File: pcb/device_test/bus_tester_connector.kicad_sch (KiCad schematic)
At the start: 7 parts, among them J301 USB_C_Receptacle_USB2.0_16P, J302 Conn_02x10_Row_Letter_First

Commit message: update ALL parts
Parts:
- C301: footprint Capacitor_Tantalum_SMD:CP_EIA-7343-43_Kemet-X_Pad2.25x2.55mm_HandSolder -> Capacitor_Tantalum_SMD:CP_EIA-7343-43_Kemet-X; LCSC C7230 -> C132558
- J302: MOUSER (none) -> 798-PCN10C20S254DS72
- R303: value 390 -> 1k; LCSC C17655 -> C17513
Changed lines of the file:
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@@
 			)
 		)
-		(property "Footprint" "Capacitor_Tantalum_SMD:CP_EIA-7343-43_Kemet-X_Pad2.25x2.55mm_HandSolder"
+		(property "Footprint" "Capacitor_Tantalum_SMD:CP_EIA-7343-43_Kemet-X"
 			(at 122.8852 67.31 0)
 			(effects
@@
 			)
 		)
-		(property "LCSC" "C7230"
+		(property "LCSC" "C132558"
 			(at 121.92 63.5 0)
 			(effects
@@
 				)
 				(hide yes)
+			)
+		)
+		(property "MOUSER" ""
+			(at 121.92 63.5 0)
+			(effects
+				(font
+					(size 1.27 1.27)
+				)
 			)
 		)
@@
 			)
 		)
-		(property "Value" "390"
+		(property "Value" "1k"
 			(at 146.05 99.0599 0)
 			(effects
@@
 			)
 		)
-		(property "LCSC" "C17655"
+		(property "LCSC" "C17513"
 			(at 143.51 97.79 0)
 			(effects
@@
 				)
 				(hide yes)
+			)
+		)
+		(property "MOUSER" ""
+			(at 143.51 97.79 0)
+			(effects
+				(font
+					(size 1.27 1.27)
+				)
 			)
 		)
@@
 			)
 		)
+		(property "MOUSER" ""
+			(at 73.66 86.36 0)
+			(effects
+				(font
+					(size 1.27 1.27)
+				)
+			)
+		)
 		(pin "B1"
 		)
@@
 			)
 		)
+		(property "MOUSER" "798-PCN10C20S254DS72"
+			(at 187.96 87.63 0)
+			(effects
+				(font
+					(size 1.27 1.27)
+				)
+			)
+		)
 		(pin "b2"
 		)
@@
 			)
 		)
+		(property "MOUSER" ""
+			(at 115.57 96.52 0)
+			(effects
+				(font
+					(size 1.27 1.27)
+				)
+			)
+		)
 		(pin "1"
 		)
@@
 			)
 		)
+		(property "MOUSER" ""
+			(at 143.51 87.63 0)
+			(effects
+				(font
+					(size 1.27 1.27)
+				)
+			)
+		)
 		(pin "2"
 		)
@@
 			)
 		)
+		(property "MOUSER" ""
+			(at 127 96.52 0)
+			(effects
+				(font
+					(size 1.27 1.27)
+				)
+			)
+		)

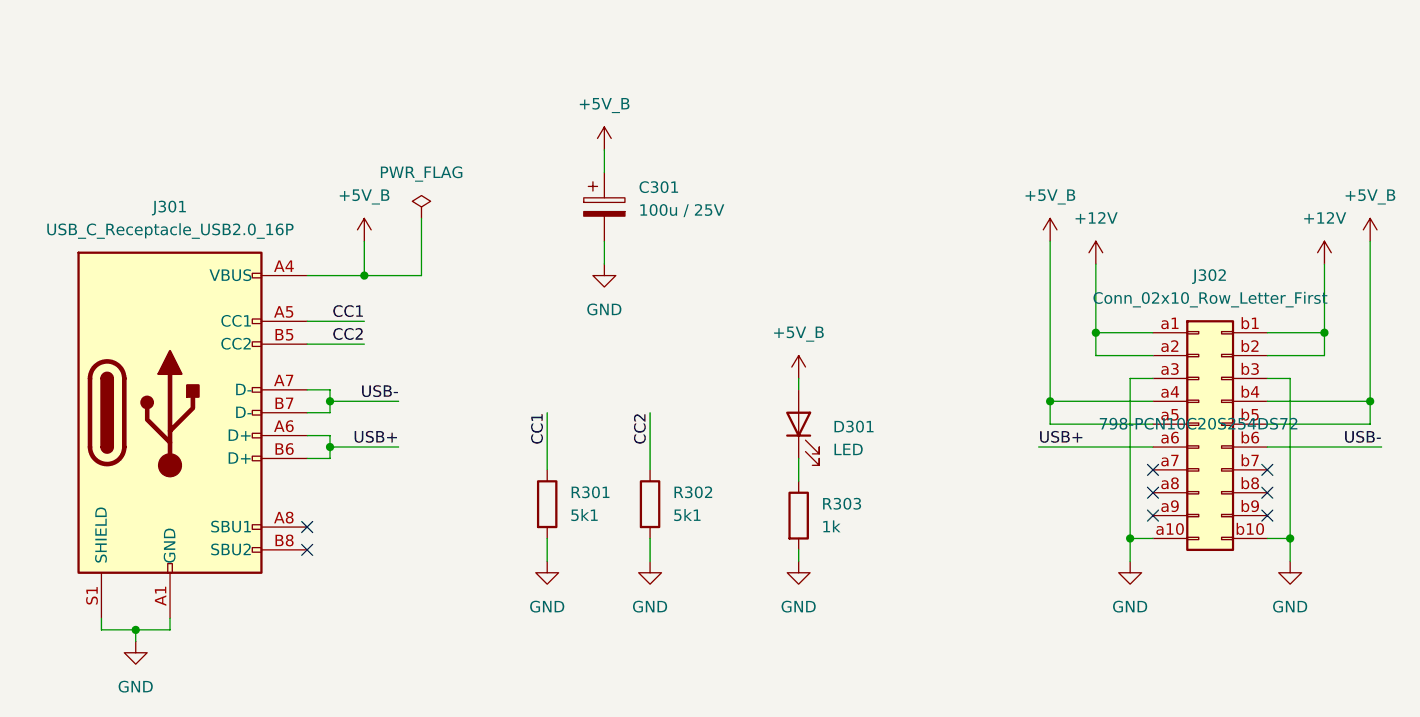
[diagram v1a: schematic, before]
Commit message: fix device tester pcb
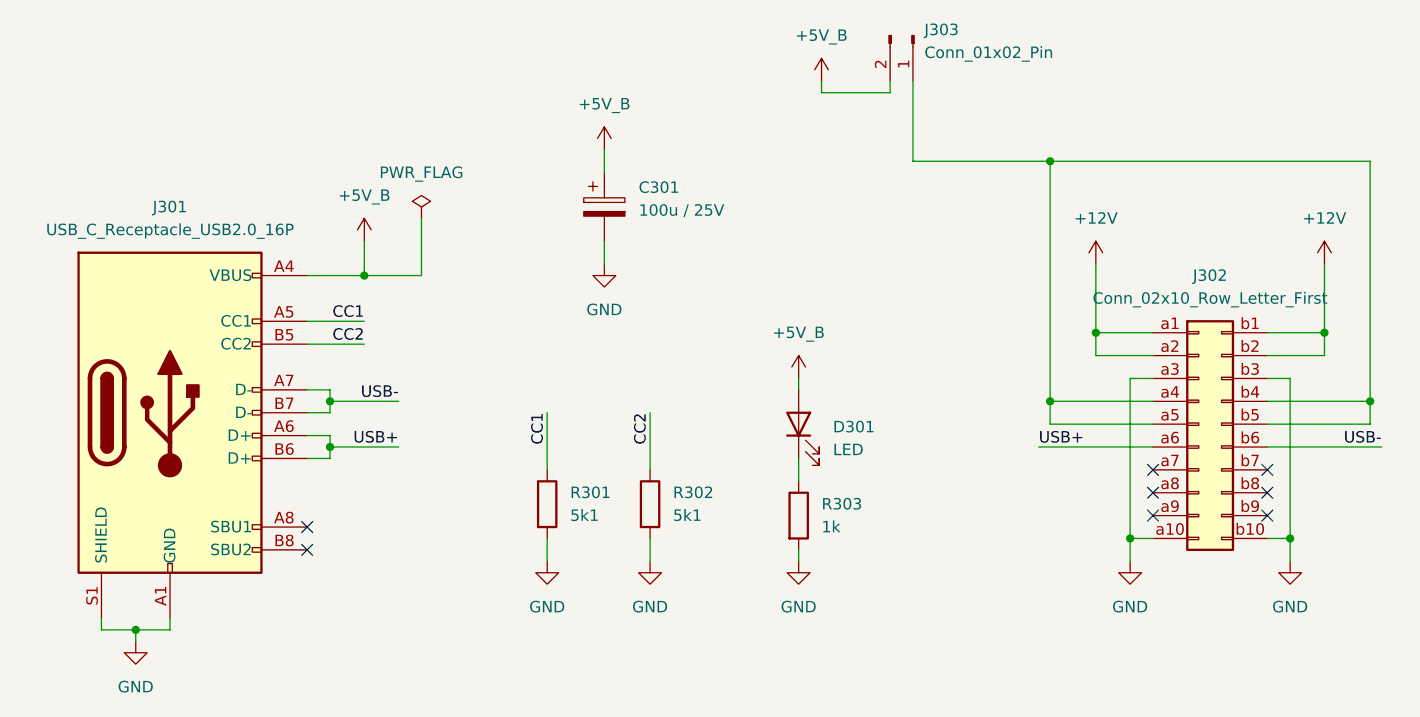
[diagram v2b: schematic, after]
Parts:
- added J303: Conn_01x02_Pin, Connector_PinHeader_2.54mm:PinHeader_1x02_P2.54mm_Vertical, symbol Connector:Conn_01x02_Pin
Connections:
- net +5V_B: now also J303.2 (Pin_2); no longer J302.a4 (Pin_a4), J302.a5 (Pin_a5), J302.b4 (Pin_b4), J302.b5 (Pin_b5)
- new net: J302.a4 (Pin_a4), J302.a5 (Pin_a5), J302.b4 (Pin_b4), J302.b5 (Pin_b5), J303.1 (Pin_1)
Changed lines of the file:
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@@
+	)
+	(junction
+		(at 171.45 58.42)
+		(diameter 0)
+		(color 0 0 0 0)
 	)
 	(junction
@@
 	(wire
 		(pts
-			(xy 171.45 85.09) (xy 171.45 67.31)
+			(xy 171.45 58.42) (xy 171.45 85.09)
 		)
 		(stroke
@@
 	(wire
 		(pts
+			(xy 207.01 58.42) (xy 207.01 85.09)
+		)
+		(stroke
+			(width 0)
+			(type default)
+		)
+	)
+	(wire
+		(pts
+			(xy 153.67 49.53) (xy 153.67 50.8)
+		)
+		(stroke
+			(width 0)
+			(type default)
+		)
+	)
+	(wire
+		(pts
 			(xy 91.44 90.17) (xy 99.06 90.17)
 		)
@@
 	(wire
 		(pts
+			(xy 207.01 58.42) (xy 171.45 58.42)
+		)
+		(stroke
+			(width 0)
+			(type default)
+		)
+	)
+	(wire
+		(pts
 			(xy 91.44 86.36) (xy 91.44 85.09)
 		)
@@
 	(wire
 		(pts
-			(xy 207.01 85.09) (xy 207.01 67.31)
-		)
-		(stroke
-			(width 0)
-			(type default)
-		)
-	)
-	(wire
-		(pts
 			(xy 195.58 82.55) (xy 198.12 82.55)
 		)
@@
 	(wire
 		(pts
+			(xy 171.45 58.42) (xy 156.21 58.42)
+		)
+		(stroke
+			(width 0)
+			(type default)
+		)
+	)
+	(wire
+		(pts
+			(xy 156.21 58.42) (xy 156.21 49.53)
+		)
+		(stroke
+			(width 0)
+			(type default)
+		)
+	)
+	(wire
+		(pts
 			(xy 201.93 77.47) (xy 201.93 69.85)
 		)
@@
 	(wire
 		(pts
+			(xy 146.05 50.8) (xy 146.05 49.53)
+		)
+		(stroke
+			(width 0)
+			(type default)
+		)
+	)
+	(wire
+		(pts
 			(xy 73.66 109.22) (xy 73.66 110.49)
 		)
@@
 		(pts
 			(xy 69.85 110.49) (xy 73.66 110.49)
+		)
+		(stroke
+			(width 0)
+			(type default)
+		)
+	)
+	(wire
+		(pts
+			(xy 153.67 50.8) (xy 146.05 50.8)
 		)
 		(stroke
@@
 	)
 	(symbol
-		(lib_id "power:+12V")
-		(at 207.01 67.31 0)
+		(lib_id "Connector:Conn_01x02_Pin")
+		(at 156.21 44.45 270)
 		(unit 1)
 		(exclude_from_sim no)
@@
 		(dnp no)
 		(fields_autoplaced yes)
-		(property "Reference" "#PWR0312"
-			(at 207.01 71.12 0)
-			(effects
-				(font
-					(size 1.27 1.27)
-				)
-				(hide yes)
-			)
-		)
-		(property "Value" "+5V_B"
-			(at 207.01 62.23 0)
-			(effects
-				(font
-					(size 1.27 1.27)
-				)
-			)
-		)
-		(property "Footprint" ""
-			(at 207.01 67.31 0)
-			(effects
-				(font
-					(size 1.27 1.27)
-				)
-				(hide yes)
-			)
-		)
-		(property "Datasheet" ""
-			(at 207.01 67.31 0)
-			(effects
-				(font
-					(size 1.27 1.27)
-				)
-				(hide yes)
-			)
-		)
-		(property "Description" "Power symbol creates a global label with name \"+5V\""
-			(at 207.01 67.31 0)
-			(effects
-				(font
-					(size 1.27 1.27)
-				)
-				(hide yes)
-			)
-		)
-		(property "LCSC" ""
-			(at 207.01 67.31 0)
+		(property "Reference" "J303"
+			(at 157.48 43.8149 90)
+			(effects
+				(font
+					(size 1.27 1.27)
+				)
+				(justify left)
+			)
+		)
+		(property "Value" "Conn_01x02_Pin"
+			(at 157.48 46.3549 90)
+			(effects
+				(font
+					(size 1.27 1.27)
+				)
+				(justify left)
+			)
+		)
+		(property "Footprint" "Connector_PinHeader_2.54mm:PinHeader_1x02_P2.54mm_Vertical"
+			(at 156.21 44.45 0)
+			(effects
+				(font
+					(size 1.27 1.27)
+				)
+				(hide yes)
+			)
+		)
+		(property "Datasheet" "~"
+			(at 156.21 44.45 0)
+			(effects
+				(font
+					(size 1.27 1.27)
+				)
+				(hide yes)
+			)
+		)
+		(property "Description" "Generic connector, single row, 01x02, script generated"
+			(at 156.21 44.45 0)
 			(effects
 				(font
@@
 		(pin "1"
 		)
+		(pin "2"
+		)
 		(instances
-			(project "device_test"
+			(project ""
 				(path "/5d20b266-567e-45c6-9e3e-145c2aea1daa/863e4a9e-7535-46fc-ad01-9a2c57fe0c12"
-					(reference "#PWR0312")
+					(reference "J303")
 					(unit 1)
 				)
@@
 					(size 1.27 1.27)
 				)
+				(hide yes)
 			)
 		)
@@
 				(path "/5d20b266-567e-45c6-9e3e-145c2aea1daa/863e4a9e-7535-46fc-ad01-9a2c57fe0c12"
 					(reference "J302")
+					(unit 1)
+				)
+			)
+		)
+	)
+	(symbol
+		(lib_id "power:+5V")
+		(at 146.05 49.53 0)
+		(unit 1)
+		(exclude_from_sim no)
+		(in_bom yes)
+		(on_board yes)
+		(dnp no)
+		(fields_autoplaced yes)
+		(property "Reference" "#PWR0307"
+			(at 146.05 53.34 0)
+			(effects
+				(font
+					(size 1.27 1.27)
+				)
+				(hide yes)
+			)
+		)
+		(property "Value" "+5V_B"
+			(at 146.05 44.45 0)
+			(effects
+				(font
+					(size 1.27 1.27)
+				)
+			)
+		)
+		(property "Footprint" ""
+			(at 146.05 49.53 0)
+			(effects
+				(font
+					(size 1.27 1.27)
+				)
+				(hide yes)
+			)
+		)
+		(property "Datasheet" ""
+			(at 146.05 49.53 0)
+			(effects
+				(font
+					(size 1.27 1.27)
+				)
+				(hide yes)
+			)
+		)
+		(property "Description" "Power symbol creates a global label with name \"+5V\""
+			(at 146.05 49.53 0)
+			(effects
+				(font
+					(size 1.27 1.27)
+				)
+				(hide yes)
+			)
+		)
+		(property "LCSC" ""
+			(at 146.05 49.53 0)
+			(effects
+				(font
+					(size 1.27 1.27)
+				)
+				(hide yes)
+			)
+		)
+		(pin "1"
+		)
+		(instances
+			(project "device_test"
+				(path "/5d20b266-567e-45c6-9e3e-145c2aea1daa/863e4a9e-7535-46fc-ad01-9a2c57fe0c12"
+					(reference "#PWR0307")
 					(unit 1)
 				)
@@
 					(unit 1)
 				)
-			)
-		)
-	)
-	(symbol
-		(lib_id "power:+12V")
-		(at 171.45 67.31 0)
-		(unit 1)
-		(exclude_from_sim no)
-		(in_bom yes)
-		(on_board yes)
-		(dnp no)
-		(fields_autoplaced yes)
-		(property "Reference" "#PWR0307"
-			(at 171.45 71.12 0)
-			(effects
-				(font
-					(size 1.27 1.27)
-				)
-				(hide yes)
-			)
-		)
-		(property "Value" "+5V_B"
-			(at 171.45 62.23 0)
-			(effects
-				(font
-					(size 1.27 1.27)
-				)
-			)
-		)
-		(property "Footprint" ""
-			(at 171.45 67.31 0)
-			(effects
-				(font
-					(size 1.27 1.27)
-				)
-				(hide yes)
-			)
-		)
-		(property "Datasheet" ""
-			(at 171.45 67.31 0)
-			(effects
-				(font
-					(size 1.27 1.27)
-				)
-				(hide yes)
-			)
-		)
-		(property "Description" "Power symbol creates a global label with name \"+5V\""
-			(at 171.45 67.31 0)
-			(effects
-				(font
-					(size 1.27 1.27)
-				)
-				(hide yes)
-			)
-		)
-		(property "LCSC" ""
-			(at 171.45 67.31 0)
-			(effects
-				(font
-					(size 1.27 1.27)
-				)
-				(hide yes)
-			)
-		)
-		(pin "1"
-		)
-		(instances
-			(project "device_test"
-				(path "/5d20b266-567e-45c6-9e3e-145c2aea1daa/863e4a9e-7535-46fc-ad01-9a2c57fe0c12"
-					(reference "#PWR0307")
-					(unit 1)
-				)
